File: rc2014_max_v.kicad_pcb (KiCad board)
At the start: 2 copper layers, 101.6 x 50.8 mm, 121 parts, among them J1 M3 Mounting Hole, J2 Conn_01x40, J3 Pro Bus, J4 Conn_01x24, J5 AVR-JTAG-10, J6 USB_B_Micro, J7 PMOD1, J8 PMOD, SW1 SW_Push, SW2 SW_Push, U1 TXB0108PWR, U10 93LCxxBxxOT, U11 MIC5356-SGYMME, U12 IS61LV5128AL-10TLI, U13 Si5351A-B-GT, U2 SN74ALVC164245DGG, U3 SN74ALVC164245DGG, U4 5M1270ZT144C5N, U5 TXB0108PWR, U6 SN74ALVC164245DGG, U7 MIC5356-SGYMME, U8 TPD2EUSB30, U9 FT2232H, X1 CB3LV-3I-50M0000, Y2 25MHZ 8PF

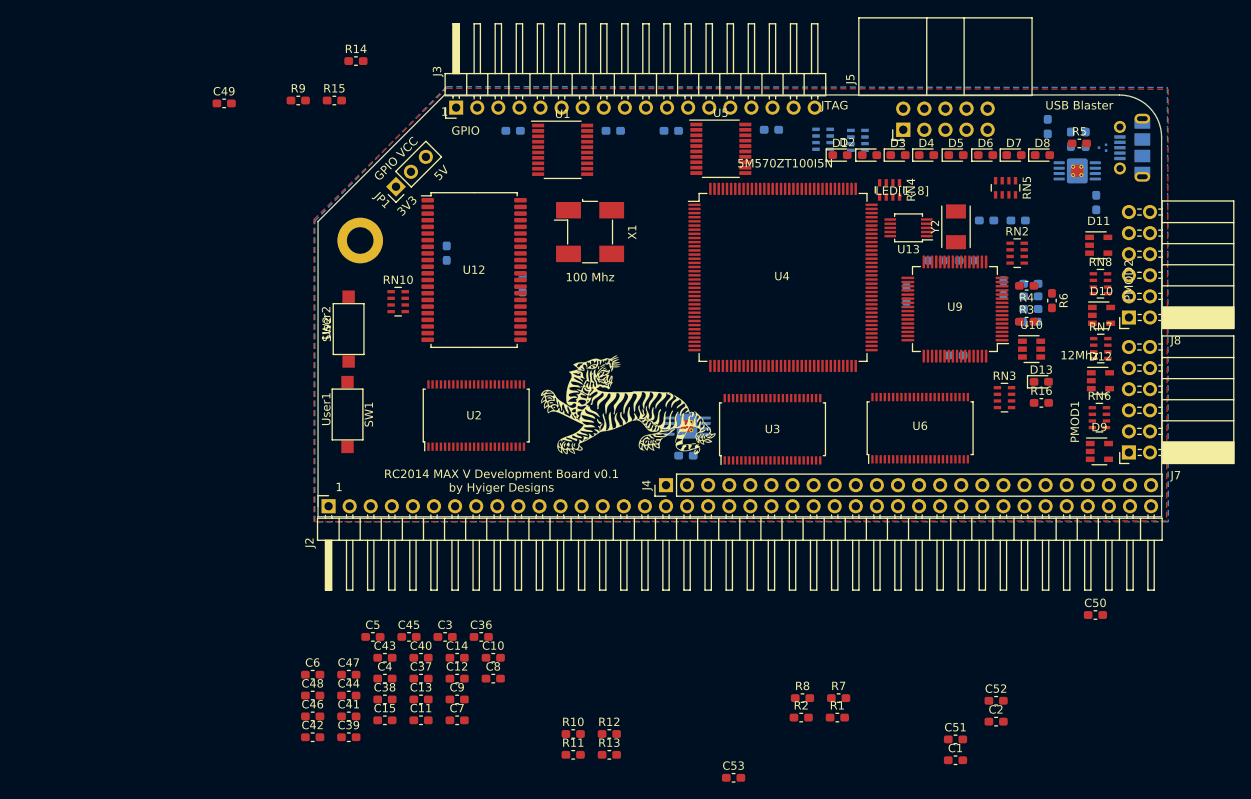
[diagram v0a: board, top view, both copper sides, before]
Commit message: updated clock
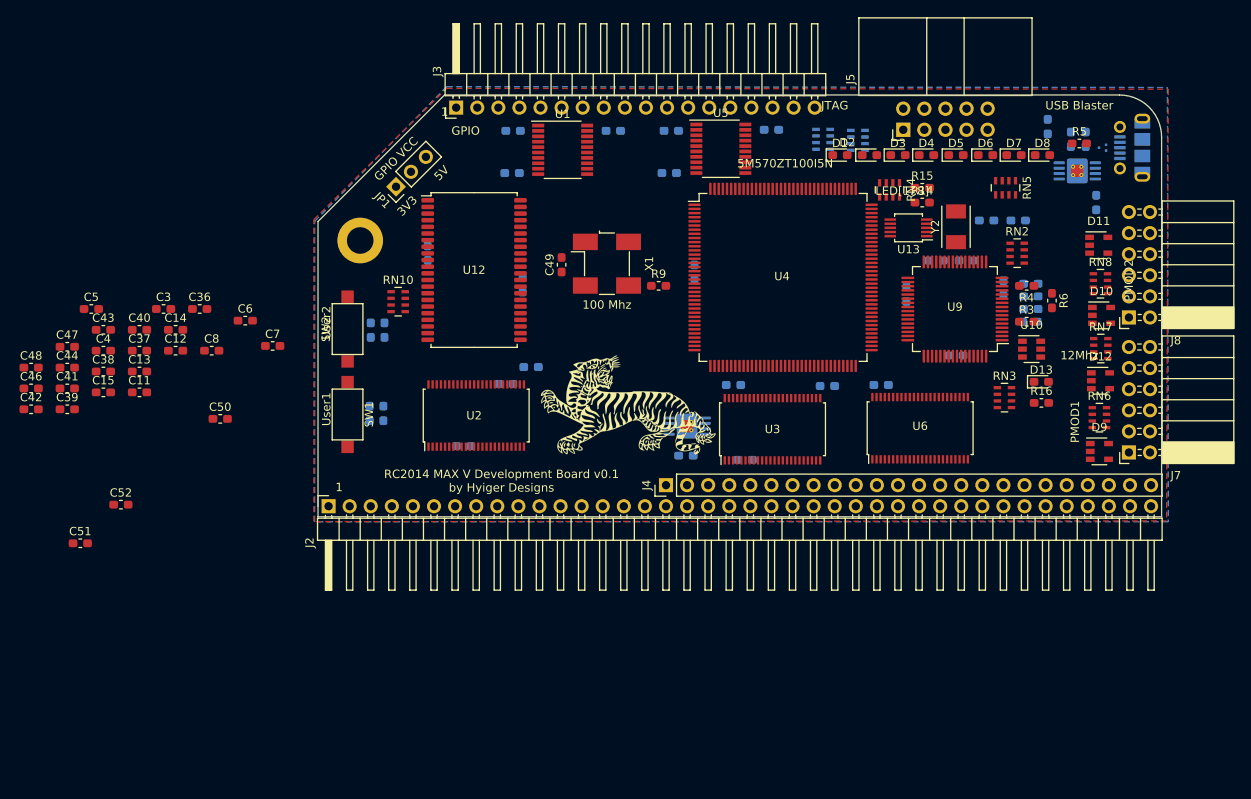
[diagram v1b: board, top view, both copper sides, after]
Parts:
- C1, C10, C2, C45, C53, C9, R1, R10, R11, R12, R13, R2, R7, R8: moved to B.Cu
- moved C50 108.0 mm to (63.7, 115.7)
- moved C52 108.0 mm to (51.7, 126.0)
- moved C51 108.0 mm to (46.8, 130.7)
- moved C2 88.9 mm to (81.8, 105.0), turned to 270 degrees
- moved C1 82.0 mm to (81.7, 115.1), turned to 90 degrees
- moved R1 76.4 mm to (98.8, 86.1), turned to 180 degrees
- moved R15 71.6 mm to (148.2, 87.9)
- moved R14 70.3 mm to (148.2, 89.7)
- moved R2 67.5 mm to (117.7, 86.1), turned to 180 degrees
- moved R8 67.1 mm to (83.4, 105.0), turned to 90 degrees
- moved R7 64.7 mm to (83.3, 115.1), turned to 270 degrees
- moved R11 58.0 mm to (143.3, 111.6)
- moved C45 55.8 mm to (120.8, 98.0), turned to 90 degrees
- moved C53 54.8 mm to (98.0, 111.5)
- moved C13 52.1 mm to (53.9, 110.0)
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
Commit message: organized bypass caps
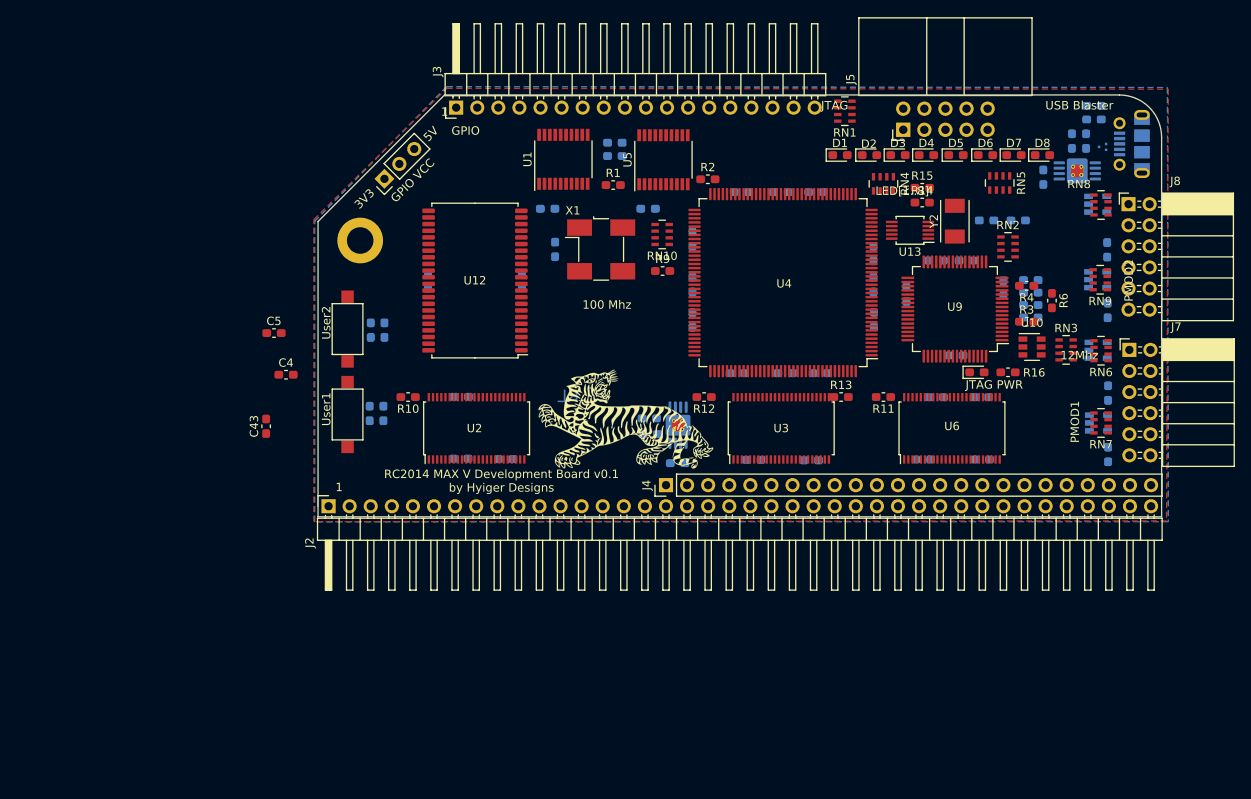
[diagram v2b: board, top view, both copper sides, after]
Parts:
- removed C52, C53: 100nF, Capacitor_SMD:C_0603_1608Metric_Pad1.05x0.95mm_HandSolder
- added C27: 100nF, Capacitor_SMD:C_0603_1608Metric_Pad1.05x0.95mm_HandSolder, B.Cu at (170.5, 95.4)
- added C28: 100nF, Capacitor_SMD:C_0603_1608Metric_Pad1.05x0.95mm_HandSolder, B.Cu at (170.5, 102.7)
- C11, C12, C13, C14, C15, C3, C36, C37, C38, C39, C40, C41, C42, C44, C46, C47, C48, C49, C50, C51, C6, C7, C8, D10, D11, D12, D9, R5: moved to B.Cu
- R1, R10, R11, R12, R13, R2, RN1, RN9: moved to F.Cu
- RN4, RN5: value 200R -> 270R
- X1: value CB3LV-3I-50M0000 -> CB3LV-3I-100M0000
- moved C51 124.2 mm to (170.6, 120.0), turned to 90 degrees
- moved C39 110.1 mm to (155.3, 113.1)
- moved C42 109.0 mm to (149.9, 113.1)
- moved C50 107.0 mm to (170.6, 112.6), turned to 90 degrees
- moved C12 98.0 mm to (155.4, 120.6)
- moved C15 93.7 mm to (142.3, 99.6), turned to 270 degrees
- moved C38 93.0 mm to (142.4, 103.8), turned to 90 degrees
- moved C14 91.4 mm to (148.3, 120.6), turned to 180 degrees
- moved C46 90.8 mm to (131.7, 110.2)
- moved C44 88.5 mm to (131.2, 88.4)
- moved C3 85.8 mm to (142.3, 95.8), turned to 90 degrees
- moved C40 82.2 mm to (135.9, 110.2), turned to 180 degrees
- moved C11 81.3 mm to (134.8, 120.7)
- moved C41 75.8 mm to (120.5, 103.8), turned to 90 degrees
- moved C8 75.2 mm to (135.4, 88.4), turned to 180 degrees
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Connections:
- net DIR renamed DIR_A
- net IO1_CLK0 renamed CLK_100Mhz
- net OE_D1 renamed OE_D
- J2 pad 35: TX_A -> (no net)
- J2 pad 37: Net-(J2-Pad37) -> (no net)
- J2 pad 38: Net-(J2-Pad38) -> (no net)
- J2 pad 39: Net-(J2-Pad39) -> (no net)
- J2 pad 40: Net-(J2-Pad40) -> (no net)
- J4 pad 19: TX_B -> (no net)
- J4 pad 20: RX_B -> (no net)
- J4 pad 21: Net-(J4-Pad21) -> (no net)
- J4 pad 22: Net-(J4-Pad22) -> (no net)
- J4 pad 23: Net-(J4-Pad23) -> (no net)
- J4 pad 24: Net-(J4-Pad24) -> (no net)
- J4 pad 3: ~RFSH -> (no net)
- J4 pad 5: CLK2 -> (no net)
- J5 pad 7: Net-(J5-Pad7) -> (no net)
- J5 pad 8: Net-(J5-Pad8) -> (no net)
- RN10 pad 4: Net-(RN10-Pad4) -> (no net)
- RN3 pad 4: Net-(RN3-Pad4) -> (no net)
- RN8 pad 1: Net-(D11-Pad1) -> Net-(D11-Pad5)
- RN8 pad 2: Net-(D11-Pad3) -> Net-(D11-Pad4)
- RN8 pad 3: Net-(D11-Pad4) -> Net-(D11-Pad3)
- RN8 pad 4: Net-(D11-Pad5) -> Net-(D11-Pad1)
- RN9 pad 1: Net-(D12-Pad1) -> Net-(D12-Pad5)
- RN9 pad 2: Net-(D12-Pad3) -> Net-(D12-Pad4)
- RN9 pad 3: Net-(D12-Pad4) -> Net-(D12-Pad3)
- RN9 pad 4: Net-(D12-Pad5) -> Net-(D12-Pad1)
- RN9 pad 5: PMOD2_5 -> PMOD2_8
- RN9 pad 6: PMOD2_6 -> PMOD2_7
- RN9 pad 7: PMOD2_7 -> PMOD2_6
- RN9 pad 8: PMOD2_8 -> PMOD2_5
- U11 pad 6: Net-(U11-Pad6) -> (no net)
- U12 pad 1: Net-(U12-Pad1) -> (no net)
- U12 pad 2: Net-(U12-Pad2) -> (no net)
- U12 pad 21: Net-(U12-Pad21) -> (no net)
- U12 pad 22: Net-(U12-Pad22) -> (no net)
- U12 pad 23: Net-(U12-Pad23) -> (no net)
- U12 pad 24: Net-(U12-Pad24) -> (no net)
- U12 pad 25: Net-(U12-Pad25) -> (no net)
- U12 pad 39: Net-(U12-Pad39) -> (no net)
- U12 pad 40: Net-(U12-Pad40) -> (no net)
- U12 pad 41: Net-(U12-Pad41) -> (no net)
- U12 pad 42: Net-(U12-Pad42) -> (no net)
- U12 pad 43: Net-(U12-Pad43) -> (no net)
- U12 pad 44: Net-(U12-Pad44) -> (no net)
- U3 pad 1: DIR_C_O -> (no net)
- U3 pad 24: DIR_C_I -> (no net)
- U3 pad 30: ~RD_F -> (no net)
- U3 pad 32: ~WR_F -> (no net)
- U3 pad 33: ~MREQ_F -> (no net)
- U3 pad 36: ~M1_F -> (no net)
- U3 pad 37: RX_A_F -> (no net)
- U3 pad 5: ~RESET2 -> (no net)
- U4 pad 1: ~WE~_RAM -> PMOD1_8
- U4 pad 101: PMOD1_3 -> A7_F
- U4 pad 102: PMOD1_4 -> A6_F
- U4 pad 103: PMOD1_5 -> A5_F
- U4 pad 104: PMOD1_6 -> A4_F
- U4 pad 105: PMOD1_7 -> A3_F
- U4 pad 106: PMOD1_8 -> A2_F
- U4 pad 107: PMOD2_1 -> A1_F
- U4 pad 108: PMOD2_2 -> A0_F
- U4 pad 109: PMOD2_3 -> ~RESET2_F
- U4 pad 110: PMOD2_4 -> ~HALT_F
- U4 pad 111: PMOD2_5 -> ~BUSRQ_F
- U4 pad 112: PMOD2_6 -> ~WAIT_F
- U4 pad 113: PMOD2_7 -> ~NMI_F
- U4 pad 114: PMOD2_8 -> ~BUSACK_F
- U4 pad 117: LED8 -> ~PAGE_F
- U4 pad 118: LED7 -> ~IORQ_F
- U4 pad 119: LED6 -> (no net)
- U4 pad 12: A13_F -> PMOD2_5
- U4 pad 120: LED5 -> (no net)
- U4 pad 121: LED4 -> (no net)
- U4 pad 122: LED3 -> (no net)
- U4 pad 123: LED2 -> (no net)
- U4 pad 124: LED1 -> (no net)
- U4 pad 125: GPIO_1_F -> D0_F
- U4 pad 127: GPIO_2_F -> D1_F
- U4 pad 129: GPIO_3_F -> D2_F
- U4 pad 13: A14_F -> PMOD2_6
- U4 pad 130: GPIO_4_F -> D3_F
- U4 pad 131: GPIO_5_F -> D4_F
- U4 pad 132: GPIO_6_F -> D5_F
- U4 pad 133: GPIO_7_F -> D6_F
- U4 pad 134: GPIO_8_F -> D7_F
- U4 pad 137: GPIO_9_F -> D8_F
- U4 pad 138: GPIO_10_F -> D9_F
- U4 pad 139: GPIO_11_F -> D10_F
- U4 pad 14: A15_F -> PMOD2_7
- U4 pad 140: GPIO_12_F -> D11_F
- U4 pad 141: GPIO_13_F -> D12_F
- U4 pad 142: GPIO_14_F -> D13_F
- U4 pad 143: GPIO_15_F -> D14_F
- U4 pad 144: GPIO_16_F -> D15_F
- U4 pad 15: A4_F -> PMOD2_8
- U4 pad 16: A5_F -> PMOD2_1
- U4 pad 18: CLK_50Mhz -> CLK_7_3728_Mhz
- U4 pad 2: ~OE~_RAM -> PMOD1_7
- U4 pad 20: CLK_7_3728_Mhz -> CLK_50Mhz
- U4 pad 21: A6_F -> PMOD2_2
- U4 pad 22: A7_F -> PMOD2_3
- U4 pad 23: A8_F -> PMOD2_4
- U4 pad 24: A9_F -> (no net)
- U4 pad 27: A0_F -> (no net)
- U4 pad 28: A1_F -> (no net)
- U4 pad 29: A2_F -> (no net)
- U4 pad 3: ~CE~_RAM -> PMOD1_6
- U4 pad 30: A3_F -> (no net)
- U4 pad 37: ~RESET2_F -> LED8
- U4 pad 38: ~HALT_F -> LED7
- U4 pad 39: ~BUSRQ_F -> LED6
- U4 pad 4: Net-(U4-Pad4) -> PMOD1_5
- U4 pad 40: ~WAIT_F -> LED5
- U4 pad 41: ~NMI_F -> LED4
- U4 pad 42: ~BUSACK_F -> LED3
- U4 pad 43: ~PAGE_F -> LED2
- U4 pad 44: ~IORQ_F -> LED1
- U4 pad 45: ~RD_F -> (no net)
- U4 pad 48: ~WR_F -> (no net)
- U4 pad 49: ~MREQ_F -> (no net)
- U4 pad 5: Net-(U4-Pad5) -> PMOD1_1
- U4 pad 50: ~M1_F -> (no net)
- U4 pad 51: Net-(U4-Pad51) -> (no net)
- U4 pad 52: Net-(U4-Pad52) -> (no net)
- U4 pad 53: D0_F -> (no net)
- U4 pad 55: D1_F -> (no net)
- U4 pad 57: D2_F -> (no net)
- U4 pad 58: D3_F -> (no net)
- U4 pad 59: D4_F -> (no net)
- U4 pad 6: A10_F -> PMOD1_2
- U4 pad 60: D5_F -> (no net)
- U4 pad 61: D6_F -> (no net)
- U4 pad 62: D7_F -> (no net)
- U4 pad 63: D8_F -> GPIO_16_F
- U4 pad 66: D9_F -> GPIO_15_F
- U4 pad 67: D10_F -> GPIO_14_F
- U4 pad 68: D11_F -> GPIO_13_F
- U4 pad 69: D12_F -> GPIO_12_F
- U4 pad 7: A11_F -> PMOD1_3
- U4 pad 70: D13_F -> GPIO_11_F
- U4 pad 71: D14_F -> GPIO_10_F
- U4 pad 72: D15_F -> GPIO_9_F
- U4 pad 73: Net-(U4-Pad73) -> GPIO_8_F
- U4 pad 74: Net-(U4-Pad74) -> GPIO_7_F
- U4 pad 75: Net-(U4-Pad75) -> GPIO_6_F
- U4 pad 76: Net-(U4-Pad76) -> GPIO_5_F
- U4 pad 77: Net-(U4-Pad77) -> GPIO_4_F
- U4 pad 79: Net-(U4-Pad79) -> GPIO_3_F
- U4 pad 8: A12_F -> PMOD1_4
- U4 pad 80: Net-(U4-Pad80) -> GPIO_2_F
- U4 pad 81: Net-(U4-Pad81) -> GPIO_1_F
- U4 pad 84: Net-(U4-Pad84) -> ~OE~_RAM
- U4 pad 85: Net-(U4-Pad85) -> ~WE~_RAM
- U4 pad 86: Net-(U4-Pad86) -> ~CE~_RAM
- U4 pad 87: Net-(U4-Pad87) -> A15_F
- U4 pad 88: Net-(U4-Pad88) -> A14_F
- U4 pad 93: Net-(U4-Pad93) -> A13_F
- U4 pad 94: Net-(U4-Pad94) -> A12_F
- U4 pad 95: Net-(U4-Pad95) -> A11_F
- U4 pad 96: Net-(U4-Pad96) -> A10_F
- U4 pad 97: PMOD1_1 -> A9_F
- U4 pad 98: PMOD1_2 -> A8_F
- U7 pad 6: Net-(U7-Pad6) -> (no net)
- U9 pad 21: Net-(U9-Pad21) -> (no net)
- U9 pad 22: Net-(U9-Pad22) -> (no net)
- U9 pad 23: Net-(U9-Pad23) -> (no net)
- U9 pad 24: Net-(U9-Pad24) -> (no net)
- U9 pad 26: Net-(U9-Pad26) -> (no net)
- U9 pad 27: Net-(U9-Pad27) -> (no net)
- U9 pad 28: Net-(U9-Pad28) -> (no net)
- U9 pad 29: Net-(U9-Pad29) -> (no net)
- U9 pad 3: Net-(U9-Pad3) -> (no net)
- U9 pad 30: Net-(U9-Pad30) -> (no net)
- U9 pad 32: Net-(U9-Pad32) -> (no net)
- U9 pad 33: Net-(U9-Pad33) -> (no net)
- U9 pad 34: Net-(U9-Pad34) -> (no net)
- U9 pad 36: Net-(U9-Pad36) -> (no net)
- U9 pad 38: Net-(U9-Pad38) -> (no net)
- U9 pad 39: Net-(U9-Pad39) -> (no net)
- U9 pad 40: Net-(U9-Pad40) -> (no net)
- U9 pad 41: Net-(U9-Pad41) -> (no net)
- U9 pad 43: Net-(U9-Pad43) -> (no net)
- U9 pad 44: Net-(U9-Pad44) -> (no net)
- U9 pad 45: Net-(U9-Pad45) -> (no net)
- U9 pad 46: Net-(U9-Pad46) -> (no net)
- U9 pad 48: Net-(U9-Pad48) -> (no net)
- U9 pad 49: Net-(U9-Pad49) -> (no net)
- U9 pad 50: Net-(U9-Pad50) -> (no net)
- U9 pad 52: Net-(U9-Pad52) -> (no net)
- U9 pad 53: Net-(U9-Pad53) -> (no net)
- U9 pad 54: Net-(U9-Pad54) -> (no net)
- U9 pad 55: Net-(U9-Pad55) -> (no net)
- U9 pad 57: Net-(U9-Pad57) -> (no net)
- U9 pad 58: Net-(U9-Pad58) -> (no net)
- U9 pad 59: Net-(U9-Pad59) -> (no net)
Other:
- board text added: "JTAG PWR"
- board text added: "RL"
- board text removed: "5M570ZT100I5N"

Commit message: fixed errors, connected all pins, switched to 4 layers
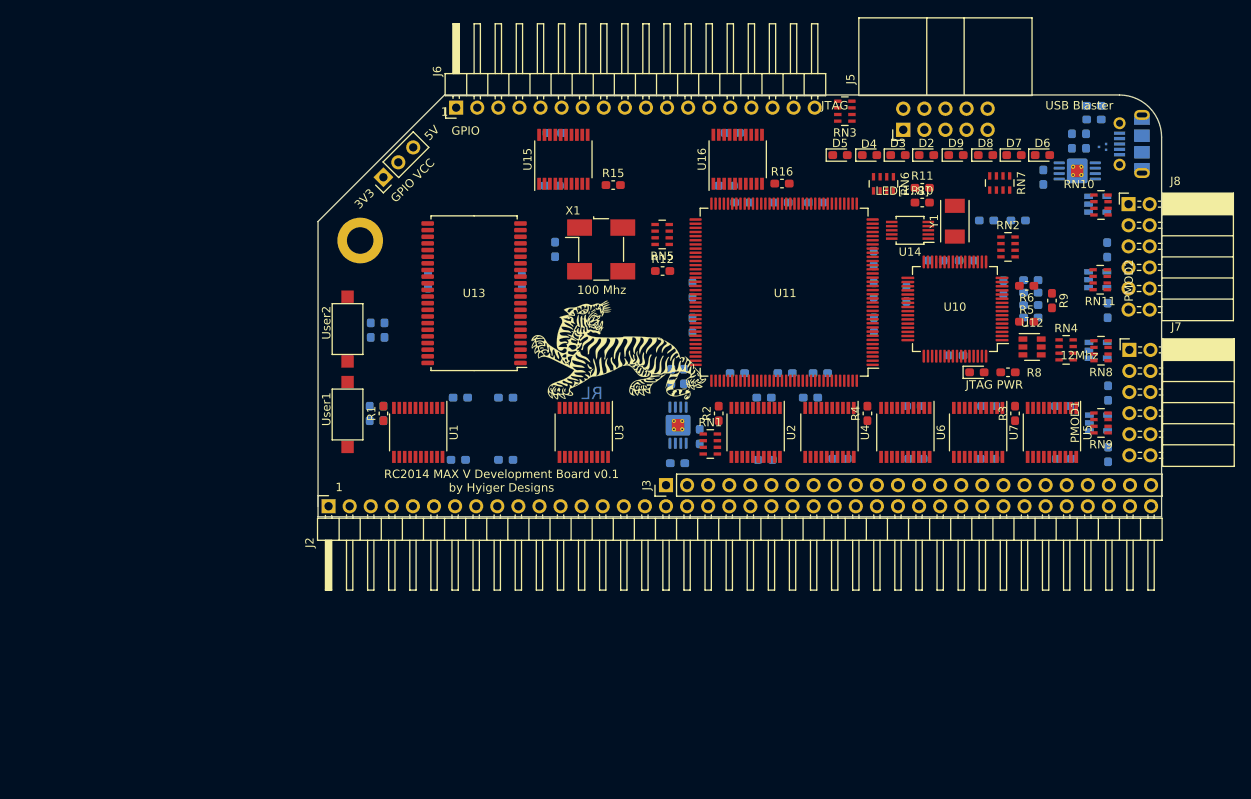
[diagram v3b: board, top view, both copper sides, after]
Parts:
- removed the R10 at (86.3, 113.1)
- removed the R11 at (143.5, 113.1)
- removed the R12 at (121.9, 113.1)
- removed the R13 at (138.4, 113.1)
- added C1: 100nF, Capacitor_SMD:C_0603_1608Metric_Pad1.05x0.95mm_HandSolder, B.Cu at (92.3, 120.7)
- added C2: 100nF, Capacitor_SMD:C_0603_1608Metric_Pad1.05x0.95mm_HandSolder, B.Cu at (98.0, 120.7)
- added R1: 1K, Resistor_SMD:R_0603_1608Metric_Pad1.05x0.95mm_HandSolder, F.Cu at (83.3, 115.1)
- added R2: 1K, Resistor_SMD:R_0603_1608Metric_Pad1.05x0.95mm_HandSolder, F.Cu at (123.7, 115.1)
- added R3: 1K, Resistor_SMD:R_0603_1608Metric_Pad1.05x0.95mm_HandSolder, F.Cu at (159.4, 115.1)
- added R4: 1K, Resistor_SMD:R_0603_1608Metric_Pad1.05x0.95mm_HandSolder, F.Cu at (141.6, 115.1)
- added RN1: 10K, Resistor_SMD:R_Array_Concave_4x0603, F.Cu at (122.7, 118.7)
- added U1: TXB0108PWR, Package_SO:TSSOP-20_4.4x6.5mm_P0.65mm, F.Cu at (87.5, 117.3)
- added U4: TXB0108PWR, Package_SO:TSSOP-20_4.4x6.5mm_P0.65mm, F.Cu at (137.0, 117.3)
- added U5: TXB0108PWR, Package_SO:TSSOP-20_4.4x6.5mm_P0.65mm, F.Cu at (163.8, 117.3)
- added U7: TXB0108PWR, Package_SO:TSSOP-20_4.4x6.5mm_P0.65mm, F.Cu at (154.9, 117.3)
- C4, C43, C5: moved to B.Cu
- U2, U3, U6: value SN74ALVC164245DGG -> TXB0108PWR; footprint Package_SO:TSSOP-48_6.1x12.5mm_P0.5mm -> Package_SO:TSSOP-20_4.4x6.5mm_P0.65mm
- moved C5 96.3 mm to (165.2, 120.5), turned to 180 degrees
- moved C4 67.5 mm to (138.3, 120.5), turned to 180 degrees
- moved C13 58.5 mm to (156.2, 114.2), turned to 180 degrees
- moved C43 52.2 mm to (121.4, 117.9)
- moved C8 49.5 mm to (92.6, 113.2), turned to 0 degrees
- moved C45 48.7 mm to (135.4, 89.7), turned to 180 degrees
- moved C6 43.7 mm to (156.1, 120.5)
- moved C7 37.7 mm to (147.4, 120.5), turned to 180 degrees
- moved U2 33.6 mm to (128.1, 117.3), turned to 270 degrees
- moved C51 33.1 mm to (126.5, 89.7), turned to 180 degrees
- moved C55 31.1 mm to (142.4, 100.2), turned to 270 degrees
- moved C3 28.1 mm to (129.3, 120.7), turned to 0 degrees
- moved C42 26.7 mm to (118.0, 110.6), turned to 90 degrees
- moved U3 23.8 mm to (107.4, 117.3), turned to 270 degrees
- moved C31 21.7 mm to (124.6, 87.6), turned to 0 degrees
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- renumbered C18 to C15, C19 to C16, C20 to C17, C21 to C18, C22 to C19, C23 to C20, C24 to C21, C25 to C22, C26 to C23, C29 to C24, C30 to C25, C31 to C26, C32 to C27, C33 to C28, C34 to C29, C35 to C30, C54 to C31, C55 to C32, C49 to C33, C16 to C34, C17 to C35, C1 to C36, C2 to C37, C27 to C38, C28 to C39, C50 to C40, C51 to C41, C15 to C42, C48 to C44, C36 to C45, C37 to C46, C38 to C47, C39 to C48, C40 to C49, C41 to C50, C42 to C51, C44 to C52, C45 to C53, C46 to C54, C47 to C55, D13 to D1, D9 to D10, D10 to D11, D11 to D12, D12 to D13, D4 to D2, D2 to D4, D1 to D5, D8 to D6, D6 to D8, D5 to D9, J4 to J3, J6 to J4, J3 to J6, R14 to R10, R15 to R11, R9 to R12, R7 to R13, R8 to R14, R1 to R15, R2 to R16, R3 to R5, R4 to R6, R5 to R7, R16 to R8, R6 to R9, RN8 to RN10, RN9 to RN11, RN1 to RN3, RN3 to RN4, RN10 to RN5, RN4 to RN6, RN5 to RN7, RN6 to RN8, RN7 to RN9, U9 to U10, U4 to U11, U10 to U12, U12 to U13, U13 to U14, U1 to U15, U5 to U16, U11 to U18, U7 to U8, U8 to U9, Y2 to Y1
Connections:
- C10 pad 1: 5V -> +3V3
- C11 pad 1: 5V -> +3V3
- C12 pad 1: 5V -> +3V3
- C13 pad 1: 5V -> +3V3
- C14 pad 1: 5V -> +3V3
- C21 pad 1: Net-(C24-Pad1) -> Net-(C21-Pad1)
- C3 pad 1: +3V3 -> 5V
- C4 pad 1: +3V3 -> 5V
- C42 pad 1: +1V8 -> 1V8
- C44 pad 1: +3V3 -> 3V3
- C45 pad 1: +3V3 -> 3V3
- C46 pad 1: +3V3 -> 3V3
- C47 pad 1: +3V3 -> 3V3
- C48 pad 1: +3V3 -> 3V3
- C49 pad 1: +3V3 -> 3V3
- C5 pad 1: +3V3 -> 5V
- C50 pad 1: +3V3 -> 3V3
- C51 pad 1: +3V3 -> 3V3
- C52 pad 1: +1V8 -> 1V8
- C53 pad 1: +1V8 -> 1V8
- C54 pad 1: +1V8 -> 1V8
- C55 pad 1: +1V8 -> 1V8
- C6 pad 1: +3V3 -> 5V
- C7 pad 1: +3V3 -> 5V
- C9 pad 1: 5V -> +3V3
- J2 pad 35: (no net) -> TXA
- J2 pad 36: RX_A -> RXA
- J3 pad 19: (no net) -> TXB
- J3 pad 20: (no net) -> RXB
- J3 pad 3: (no net) -> ~RFSH
- J3 pad 5: (no net) -> CLK2
- J4 pad 1: Net-(C24-Pad1) -> Net-(C21-Pad1)
- R15 pad 1: OE_G_1 -> OE_G
- R16 pad 1: OE_G_2 -> OE_G
- U11 pad 1: PMOD1_8 -> TXB_F
- U11 pad 100: +3V3 -> 3V3
- U11 pad 101: A7_F -> A2_F
- U11 pad 102: A6_F -> A1_F
- U11 pad 103: A5_F -> A0_F
- U11 pad 104: A4_F -> OE_A
- U11 pad 105: A3_F -> OE_C
- U11 pad 106: A2_F -> ~M1_F
- U11 pad 107: A1_F -> ~RFSH~_F
- U11 pad 108: A0_F -> ~RESET_F
- U11 pad 109: ~RESET2_F -> ~PAGE_F
- U11 pad 110: ~HALT_F -> CLK_F
- U11 pad 111: ~BUSRQ_F -> CLK2_F
- U11 pad 112: ~WAIT_F -> ~INT_F
- U11 pad 113: ~NMI_F -> ~BUSACK_F
- U11 pad 114: ~BUSACK_F -> ~MREQ_F
- U11 pad 116: +3V3 -> 3V3
- U11 pad 117: ~PAGE_F -> ~HALT_F
- U11 pad 118: ~IORQ_F -> ~WR_F
- U11 pad 119: (no net) -> ~BUSRQ_F
- U11 pad 12: PMOD2_5 -> PMOD2_6
- U11 pad 120: (no net) -> ~RD_F
- U11 pad 121: (no net) -> ~WAIT_F
- U11 pad 122: (no net) -> ~IORQ_F
- U11 pad 123: (no net) -> ~NMI_F
- U11 pad 124: (no net) -> OE_D
- U11 pad 125: D0_F -> D8_F
- U11 pad 126: +1V8 -> 1V8
- U11 pad 127: D1_F -> D0_F
- U11 pad 129: D2_F -> D9_F
- U11 pad 13: PMOD2_6 -> PMOD2_7
- U11 pad 130: D3_F -> D1_F
- U11 pad 131: D4_F -> D10_F
- U11 pad 132: D5_F -> D2_F
- U11 pad 133: D6_F -> D11_F
- U11 pad 134: D7_F -> D3_F
- U11 pad 136: +3V3 -> 3V3
- U11 pad 137: D8_F -> D12_F
- U11 pad 138: D9_F -> D4_F
- U11 pad 139: D10_F -> D13_F
- U11 pad 14: PMOD2_7 -> PMOD2_8
- U11 pad 140: D11_F -> D5_F
- U11 pad 141: D12_F -> D14_F
- U11 pad 142: D13_F -> D6_F
- U11 pad 143: D14_F -> D15_F
- U11 pad 144: D15_F -> D7_F
- U11 pad 15: PMOD2_8 -> PMOD2_1
- U11 pad 16: PMOD2_1 -> PMOD2_2
- U11 pad 19: +1V8 -> 1V8
- U11 pad 2: PMOD1_7 -> RXB_F
- U11 pad 21: PMOD2_2 -> PMOD2_3
- U11 pad 22: PMOD2_3 -> PMOD2_4
- U11 pad 23: PMOD2_4 -> PMOD1_8
- U11 pad 24: (no net) -> PMOD1_7
- U11 pad 25: +3V3 -> 3V3
- U11 pad 27: (no net) -> PMOD1_6
- U11 pad 28: (no net) -> PMOD1_5
- U11 pad 29: (no net) -> PMOD1_1
- U11 pad 3: PMOD1_6 -> TXA_F
- U11 pad 30: (no net) -> PMOD1_2
- U11 pad 31: ~RESET_F -> PMOD1_3
- U11 pad 32: ~INT_F -> PMOD1_4
- U11 pad 37: LED8 -> SCL
- U11 pad 38: LED7 -> SDA
- U11 pad 39: LED6 -> (no net)
- U11 pad 4: PMOD1_5 -> RXA_F
- U11 pad 40: LED5 -> (no net)
- U11 pad 41: LED4 -> LED8
- U11 pad 42: LED3 -> LED7
- U11 pad 43: LED2 -> LED6
- U11 pad 44: LED1 -> LED5
- U11 pad 45: (no net) -> LED4
- U11 pad 46: +3V3 -> 3V3
- U11 pad 48: (no net) -> LED3
- U11 pad 49: (no net) -> LED2
- U11 pad 5: PMOD1_1 -> OE_S
- U11 pad 50: (no net) -> LED1
- U11 pad 52: (no net) -> OE_G
- U11 pad 53: (no net) -> GPIO_16_F
- U11 pad 55: (no net) -> GPIO_15_F
- U11 pad 56: +1V8 -> 1V8
- U11 pad 57: (no net) -> GPIO_14_F
- U11 pad 58: (no net) -> GPIO_13_F
- U11 pad 59: (no net) -> GPIO_12_F
- U11 pad 6: PMOD1_2 -> (no net)
- U11 pad 60: (no net) -> GPIO_11_F
- U11 pad 61: (no net) -> GPIO_10_F
- U11 pad 62: (no net) -> GPIO_9_F
- U11 pad 63: GPIO_16_F -> GPIO_8_F
- U11 pad 64: +3V3 -> 3V3
- U11 pad 66: GPIO_15_F -> GPIO_7_F
- U11 pad 67: GPIO_14_F -> GPIO_6_F
- U11 pad 68: GPIO_13_F -> GPIO_5_F
- U11 pad 69: GPIO_12_F -> GPIO_4_F
- U11 pad 7: PMOD1_3 -> (no net)
- U11 pad 70: GPIO_11_F -> GPIO_3_F
- U11 pad 71: GPIO_10_F -> GPIO_2_F
- U11 pad 72: GPIO_9_F -> GPIO_1_F
- U11 pad 73: GPIO_8_F -> SW_USER2
- U11 pad 74: GPIO_7_F -> SW_USER1
- U11 pad 75: GPIO_6_F -> (no net)
- U11 pad 76: GPIO_5_F -> ~OE~_RAM
- U11 pad 77: GPIO_4_F -> ~WE~_RAM
- U11 pad 79: GPIO_3_F -> ~CE~_RAM
- U11 pad 8: PMOD1_4 -> PMOD2_5
- U11 pad 80: GPIO_2_F -> A15_F
- U11 pad 81: GPIO_1_F -> A13_F
- U11 pad 82: +3V3 -> 3V3
- U11 pad 84: ~OE~_RAM -> A14_F
- U11 pad 85: ~WE~_RAM -> A12_F
- U11 pad 86: ~CE~_RAM -> A11_F
- U11 pad 87: A15_F -> A10_F
- U11 pad 88: A14_F -> A9_F
- U11 pad 9: +3V3 -> 3V3
- U11 pad 90: +1V8 -> 1V8
- U11 pad 93: A13_F -> A8_F
- U11 pad 94: A12_F -> A7_F
- U11 pad 95: A11_F -> A6_F
- U11 pad 96: A10_F -> A5_F
- U11 pad 97: A9_F -> A4_F
- U11 pad 98: A8_F -> A3_F
- U15 pad 10: OE_G_1 -> OE_G
- U16 pad 10: OE_G_2 -> OE_G
- U18 pad 3: 5V -> (no net)
- U18 pad 7: +1V8 -> 1V8
- U18 pad 8: +3V3 -> 3V3
- U2 pad 1: DIR_A -> ~BUSACK_F
- U2 pad 10: GND -> OE_C
- U2 pad 11: A9 -> GND
- U2 pad 12: A8 -> ~M1
- U2 pad 13: A7 -> ~RFSH
- U2 pad 14: A6 -> ~RESET
- U2 pad 15: GND -> ~PAGE
- U2 pad 16: A5 -> CLK
- U2 pad 17: A4 -> CLK2
- U2 pad 18: 5V -> ~INT
- U2 pad 19: A3 -> 5V
- U2 pad 2: A15 -> +3V3
- U2 pad 20: A2 -> ~BUSACK
- U2 pad 3: A14 -> ~INT_F
- U2 pad 4: GND -> CLK2_F
- U2 pad 5: A13 -> CLK_F
- U2 pad 6: A12 -> ~PAGE_F
- U2 pad 7: 5V -> ~RESET_F
- U2 pad 8: A11 -> ~RFSH~_F
- U2 pad 9: A10 -> ~M1_F
- U3 pad 1: (no net) -> A0_F
- U3 pad 10: GND -> OE_A
- U3 pad 11: ~NMI -> GND
- U3 pad 12: RX_A -> A7
- U3 pad 13: ~M1 -> A6
- U3 pad 14: CLK -> A5
- U3 pad 15: GND -> A4
- U3 pad 16: ~MREQ -> A3
- U3 pad 17: ~WR -> A2
- U3 pad 18: 5V -> A1
- U3 pad 19: ~RD -> 5V
- U3 pad 2: ~RESET -> +3V3
- U3 pad 20: ~IORQ -> A0
- U3 pad 3: ~INT -> A1_F
- U3 pad 4: GND -> A2_F
- U3 pad 5: (no net) -> A3_F
- U3 pad 6: ~HALT -> A4_F
- U3 pad 7: 5V -> A5_F
- U3 pad 8: ~BUSRQ -> A6_F
- U3 pad 9: ~WAIT -> A7_F
- U6 pad 1: DIR_D -> D3_F
- U6 pad 10: GND -> OE_D
- U6 pad 11: D3 -> GND
- U6 pad 12: D11 -> D8
- U6 pad 13: D4 -> D0
- U6 pad 14: D12 -> D9
- U6 pad 15: GND -> D1
- U6 pad 16: D5 -> D10
- U6 pad 17: D13 -> D2
- U6 pad 18: 5V -> D11
- U6 pad 19: D6 -> 5V
- U6 pad 2: D0 -> +3V3
- U6 pad 20: D14 -> D3
- U6 pad 3: D8 -> D11_F
- U6 pad 4: GND -> D2_F
- U6 pad 5: D1 -> D10_F
- U6 pad 6: D9 -> D1_F
- U6 pad 7: 5V -> D9_F
- U6 pad 8: D2 -> D0_F
- U6 pad 9: D10 -> D8_F
- U8 pad 1: Net-(C24-Pad1) -> Net-(C21-Pad1)
- U8 pad 3: Net-(C24-Pad1) -> (no net)
- U8 pad 4: Net-(C24-Pad1) -> Net-(C21-Pad1)
- U8 pad 5: Net-(C24-Pad1) -> Net-(C21-Pad1)
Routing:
- removed copper zone on B.Cu, net GND
- removed copper zone on F.Cu, net GND
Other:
- copper layers 2 -> 4
